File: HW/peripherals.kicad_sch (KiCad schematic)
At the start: 13 parts, among them U3 MCP4716A0T-E

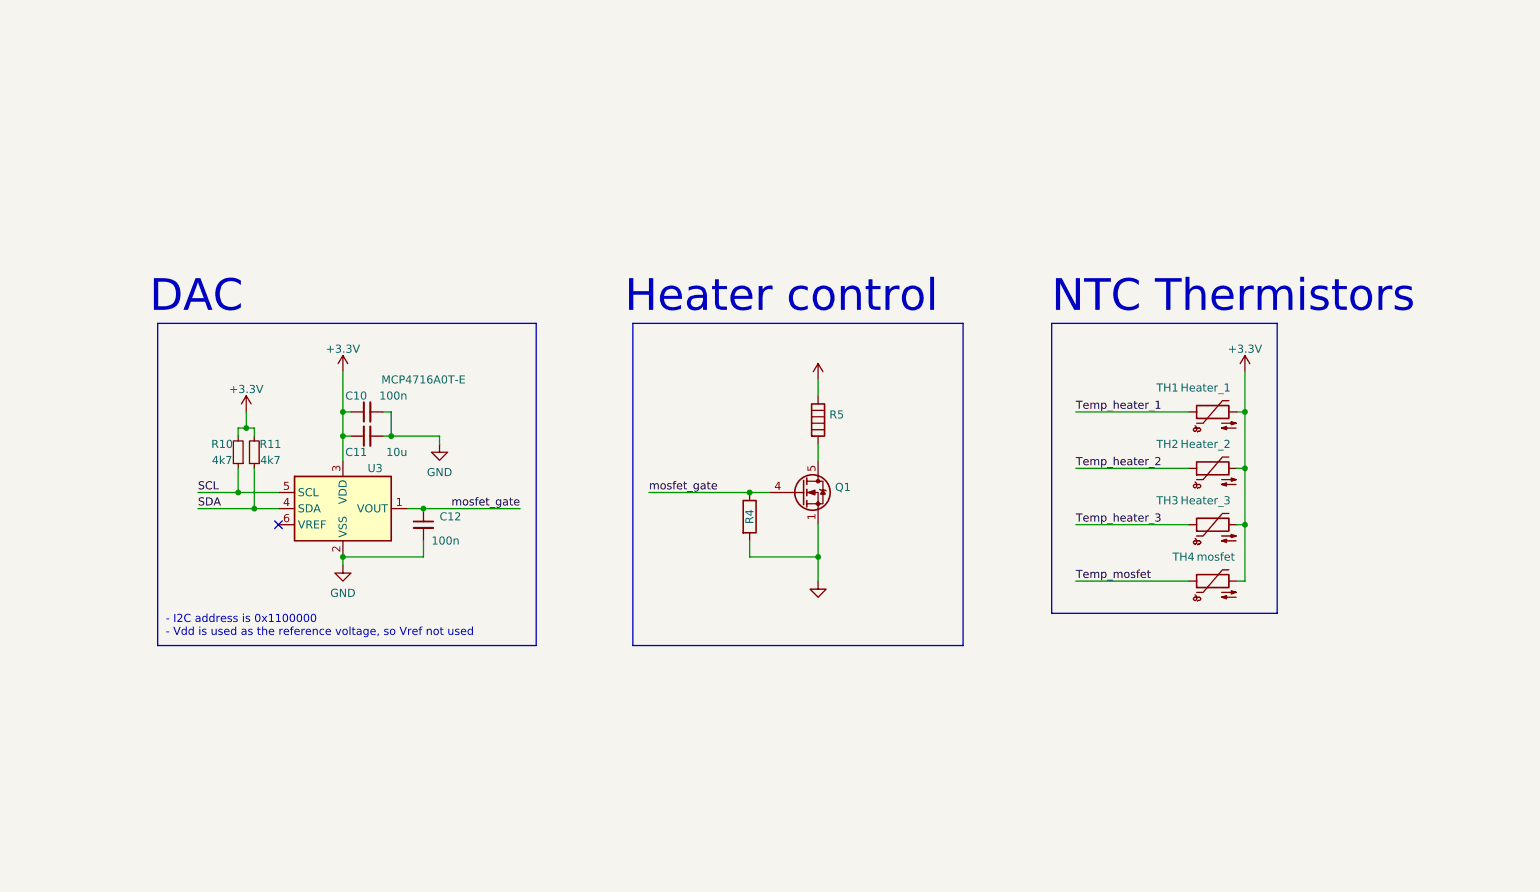
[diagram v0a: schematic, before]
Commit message: Finished sch, to be checked. Initial components layout
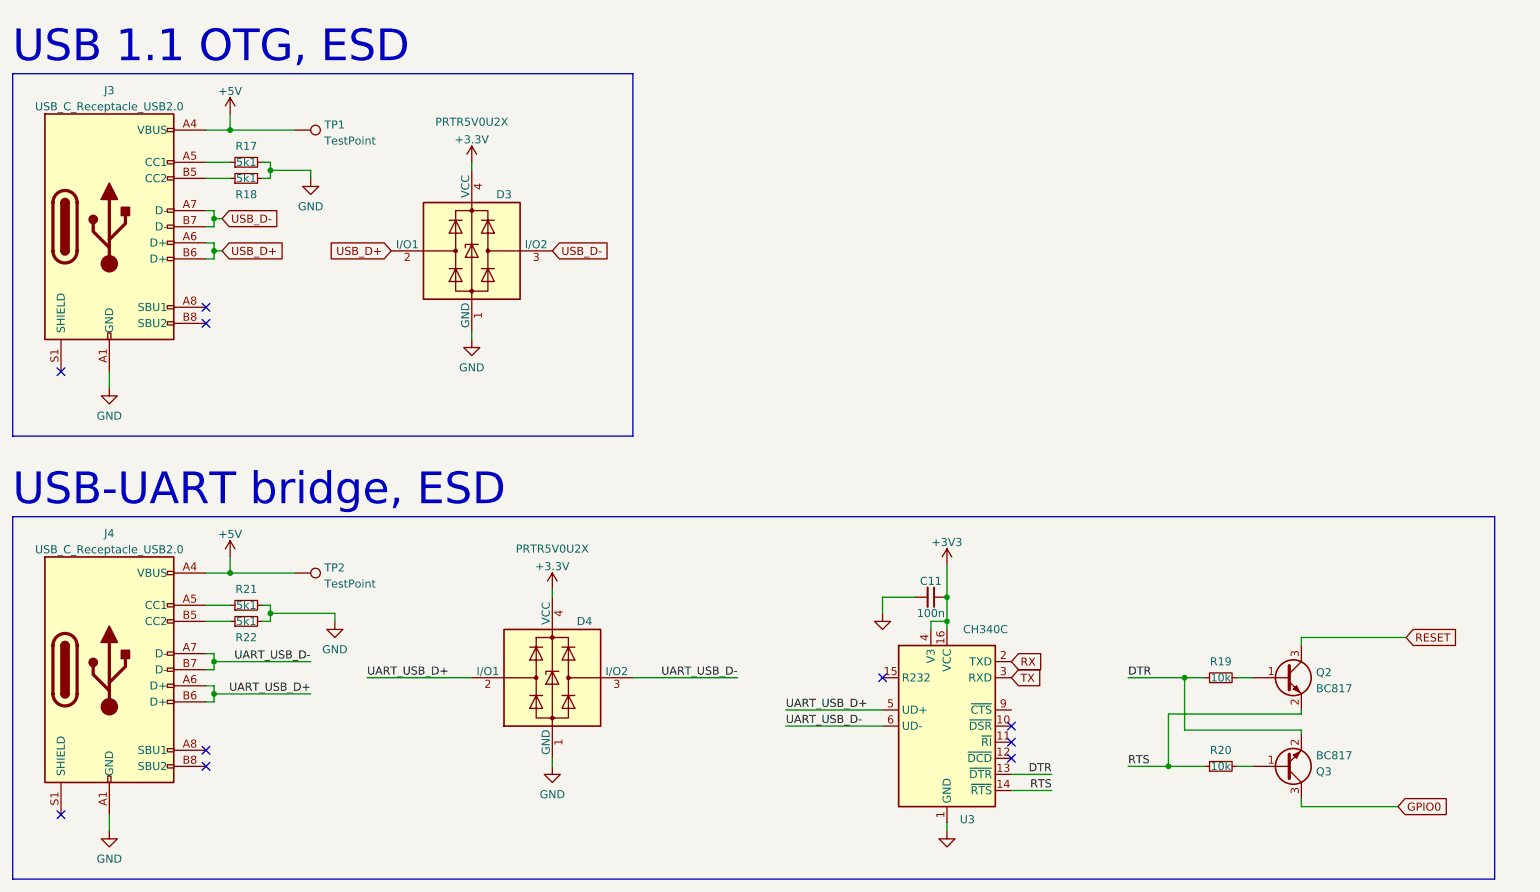
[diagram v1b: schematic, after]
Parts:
- removed C10, C12: 100n, symbol Device:C_Small
- removed Q1: (no value), symbol Transistor_FET:BUK9M156-100EX
- removed R10, R11: 4k7, symbol Device:R_Small
- removed R4: (no value), symbol Device:R
- removed R5: (no value), symbol Device:Heater
- removed TH1: Heater_1, symbol Device:Thermistor_NTC
- removed TH2: Heater_2, symbol Device:Thermistor_NTC
- removed TH3: Heater_3, symbol Device:Thermistor_NTC
- removed TH4: mosfet, symbol Device:Thermistor_NTC
- removed U3: MCP4716A0T-E, symbol MCP4716:MCP4716A0T-E
- added D3, D4: PRTR5V0U2X, Package_TO_SOT_SMD:SOT-143, symbol Power_Protection:PRTR5V0U2X
- added J3, J4: USB_C_Receptacle_USB2.0, Connector_USB:USB_C_Receptacle_HRO_TYPE-C-31-M-12, symbol Connector:USB_C_Receptacle_USB2.0
- added Q2, Q3: BC817, Package_TO_SOT_SMD:SOT-23, symbol Transistor_BJT:BC817
- added R17, R18, R21, R22: 5k1, Resistor_SMD:R_0603_1608Metric, symbol Device:R_Small
- added R19, R20: 10k, Resistor_SMD:R_0603_1608Metric, symbol Device:R_Small
- added TP1, TP2: TestPoint, TestPoint:TestPoint_Pad_3.0x3.0mm, symbol Connector:TestPoint
- added U3: CH340C, Package_SO:SOIC-16_3.9x9.9mm_P1.27mm, symbol Interface_USB:CH340C
- C11: value 10u -> 100n; footprint (none) -> Capacitor_SMD:C_0603_1608Metric
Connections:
- net +3V3: now also D3.4 (VCC), D4.4 (VCC), U3.16 (VCC), U3.4 (V3)
- net GND: now also D3.1 (GND), D4.1 (GND), J3.A1 (GND), J3.A12 (GND), J3.B1 (GND), J3.B12 (GND), J4.A1 (GND), J4.A12 (GND), J4.B1 (GND), J4.B12 (GND), R17.2, R18.2, R21.2, R22.2, U3.1 (GND)
- new net: J3.A5 (CC1), R17.1
- new net: J3.B5 (CC2), R18.1
- new net: J4.A5 (CC1), R21.1
- new net: Q2.1 (B), R19.2
- new net: Q3.1 (B), R20.2
- new net: J4.B5 (CC2), R22.1
- new net +5V: J3.A4 (VBUS), J3.A9 (VBUS), J3.B4 (VBUS), J3.B9 (VBUS), J4.A4 (VBUS), J4.A9 (VBUS), J4.B4 (VBUS), J4.B9 (VBUS), TP1.1, TP2.1
- new net DTR: Q3.2 (E), R19.1, U3.13 (~{DTR})
- new net GPIO0: Q3.3 (C)
- new net RESET: Q2.3 (C)
- new net RTS: Q2.2 (E), R20.1, U3.14 (~{RTS})
- new net RX: U3.2 (TXD)
- new net TX: U3.3 (RXD)
- new net UART_USB_D+: D4.2 (I/O1), J4.A6 (D+), J4.B6 (D+), U3.5 (UD+)
- new net UART_USB_D-: D4.3 (I/O2), J4.A7 (D-), J4.B7 (D-), U3.6 (UD-)
- new net USB_D+: D3.2 (I/O1), J3.A6 (D+), J3.B6 (D+)
- new net USB_D-: D3.3 (I/O2), J3.A7 (D-), J3.B7 (D-)
- no-connect marks 1 -> 10
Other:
- note added: "USB 1.1 OTG, ESD"
- note added: "USB-UART bridge, ESD"
- note removed: "- I2C address is 0x1100000 - Vdd is used as the reference voltage, so Vref not used"
- note removed: "DAC"
- note removed: "Heater control"
- note removed: "NTC Thermistors"

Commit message: Sch finalized, added EMC stuff, user buttons and oled
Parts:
- added J5: OLED, symbol Connector_Generic:Conn_01x04
- added R5, R6, R7: 1k, Resistor_SMD:R_0603_1608Metric, symbol Device:R_Small
- added SW1, SW4, SW5: SW_SPST, 1-1825027-1:SW_1-1825027-1, symbol Switch:SW_SPST
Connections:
- net +3V3: now also J5.3 (Pin_3)
- net GND: now also J5.4 (Pin_4), R5.2, R6.2, R7.2
- new net: R7.1, SW5.2 (B)
- new net: R5.1, SW1.2 (B)
- new net: R6.1, SW4.2 (B)
- new net SCL: J5.2 (Pin_2)
- new net SDA: J5.1 (Pin_1)
- new net temperature_minus: SW4.1 (A)
- new net temperature_plus: SW1.1 (A)
- new net user_action: SW5.1 (A)
- no-connect marks 10 -> 11
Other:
- note added: "- 4k7 pullups are integrated"
- note added: "OLED screen"
- note added: "User Buttons"

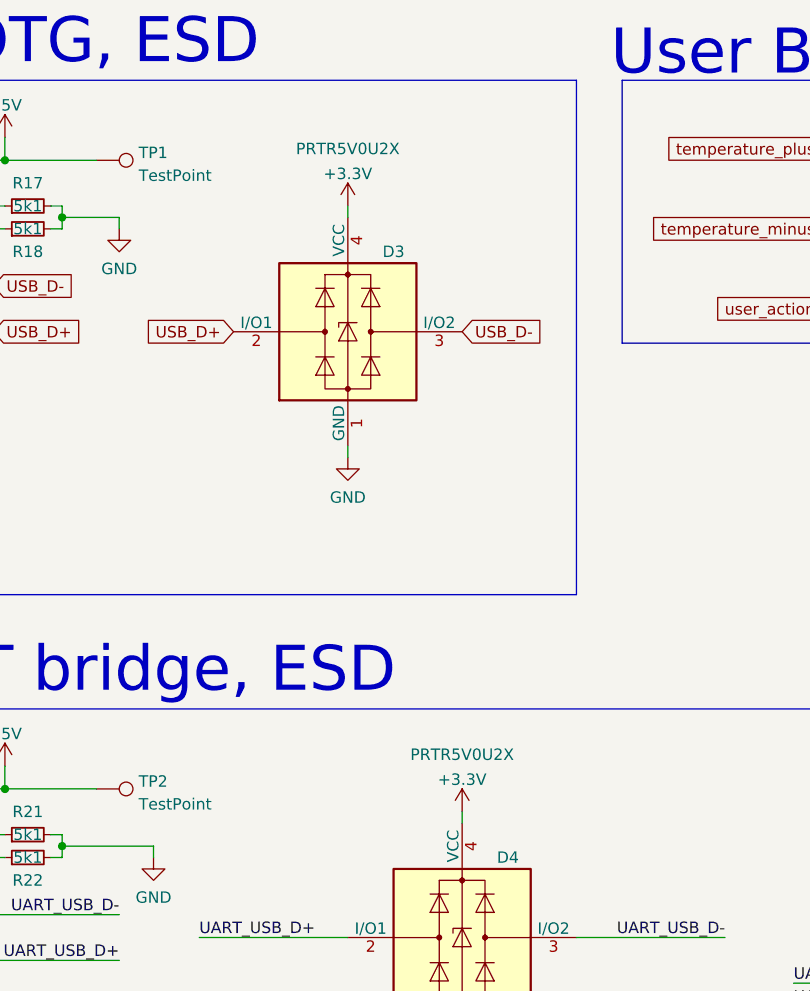
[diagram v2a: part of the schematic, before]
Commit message: Work on layout, sch fixes, added several 3d models
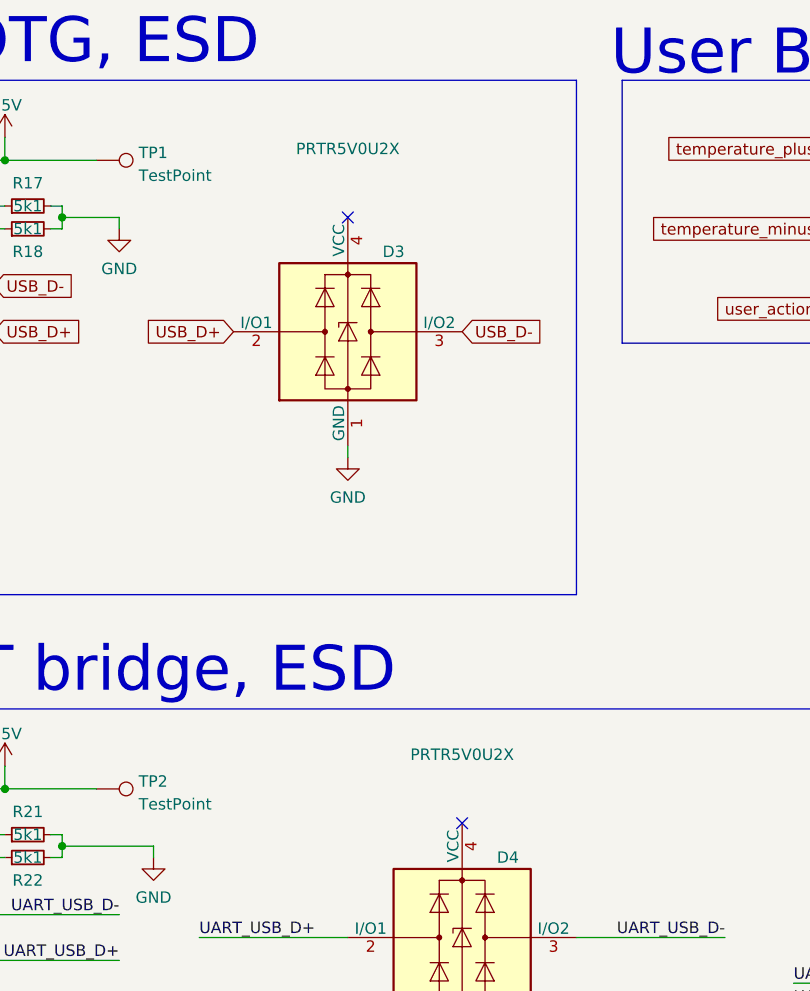
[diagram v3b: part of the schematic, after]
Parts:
- TP1, TP2: footprint TestPoint:TestPoint_Pad_3.0x3.0mm -> (none)
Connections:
- net +3V3: no longer D3.4 (VCC), D4.4 (VCC)
- no-connect marks 11 -> 13
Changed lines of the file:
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@@
   (no_connect (at 185.42 124.46))
   (no_connect (at 58.42 60.96))
+  (no_connect (at 113.03 106.68))
+  (no_connect (at 100.33 39.37))
   (no_connect (at 185.42 129.54))
   (no_connect (at 35.56 71.12))
@@
     (stroke (width 0) (type default) (color 0 0 0 0))
   )
-  (wire (pts (xy 113.03 105.41) (xy 113.03 106.68))
-    (stroke (width 0) (type default) (color 0 0 0 0))
-  )
   (wire (pts (xy 59.69 52.07) (xy 60.96 52.07))
     (stroke (width 0) (type default) (color 0 0 0 0))
@@
   )
   (wire (pts (xy 203.835 119.38) (xy 212.725 119.38))
-    (stroke (width 0) (type default) (color 0 0 0 0))
-  )
-  (wire (pts (xy 100.33 38.1) (xy 100.33 39.37))
     (stroke (width 0) (type default) (color 0 0 0 0))
   )
@@
     (pin "2")
   )
-  (symbol (lib_id "power:+3.3V") (at 100.33 38.1 0) (unit 1)
-    (in_bom yes) (on_board yes) (fields_autoplaced)
-    (property "Reference" "#PWR0128" (id 0) (at 100.33 41.91 0)
-      (effects (font (size 1.27 1.27)) hide)
-    )
-    (property "Value" "+3.3V" (id 1) (at 100.33 34.5242 0))
-    (property "Footprint" "" (id 2) (at 100.33 38.1 0)
-      (effects (font (size 1.27 1.27)) hide)
-    )
-    (property "Datasheet" "" (id 3) (at 100.33 38.1 0)
-      (effects (font (size 1.27 1.27)) hide)
-    )
-    (pin "1")
-  )
   (symbol (lib_id "power:+3V3") (at 175.26 101.6 0) (unit 1)
     (in_bom yes) (on_board yes) (fields_autoplaced)
@@
       (effects (font (size 1.27 1.27)) (justify left))
     )
-    (property "Footprint" "TestPoint:TestPoint_Pad_3.0x3.0mm" (id 2) (at 72.39 38.1 0)
+    (property "Footprint" "" (id 2) (at 72.39 38.1 0)
       (effects (font (size 1.27 1.27)) hide)
     )
@@
     (pin "S1")
   )
-  (symbol (lib_id "power:+3.3V") (at 113.03 105.41 0) (unit 1)
-    (in_bom yes) (on_board yes) (fields_autoplaced)
-    (property "Reference" "#PWR0129" (id 0) (at 113.03 109.22 0)
-      (effects (font (size 1.27 1.27)) hide)
-    )
-    (property "Value" "+3.3V" (id 1) (at 113.03 101.8342 0))
-    (property "Footprint" "" (id 2) (at 113.03 105.41 0)
-      (effects (font (size 1.27 1.27)) hide)
-    )
-    (property "Datasheet" "" (id 3) (at 113.03 105.41 0)
-      (effects (font (size 1.27 1.27)) hide)
-    )
-    (pin "1")
-  )
   (symbol (lib_id "Connector:TestPoint") (at 72.39 102.87 270) (unit 1)
     (in_bom yes) (on_board yes) (fields_autoplaced)
@@
       (effects (font (size 1.27 1.27)) (justify left))
     )
-    (property "Footprint" "TestPoint:TestPoint_Pad_3.0x3.0mm" (id 2) (at 72.39 107.95 0)
-      (effects (font (size 1.27 1.27)) hide)
-    )
+    (property "Footprint" "" (id 2) (at 72.39 107.95 0)
+      (effects (font (size 1.27 1.27)) hide)
+    )
